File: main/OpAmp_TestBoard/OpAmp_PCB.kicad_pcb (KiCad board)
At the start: 2 copper layers, 145.1 x 56.1 mm, 30 parts, among them U1 LM358

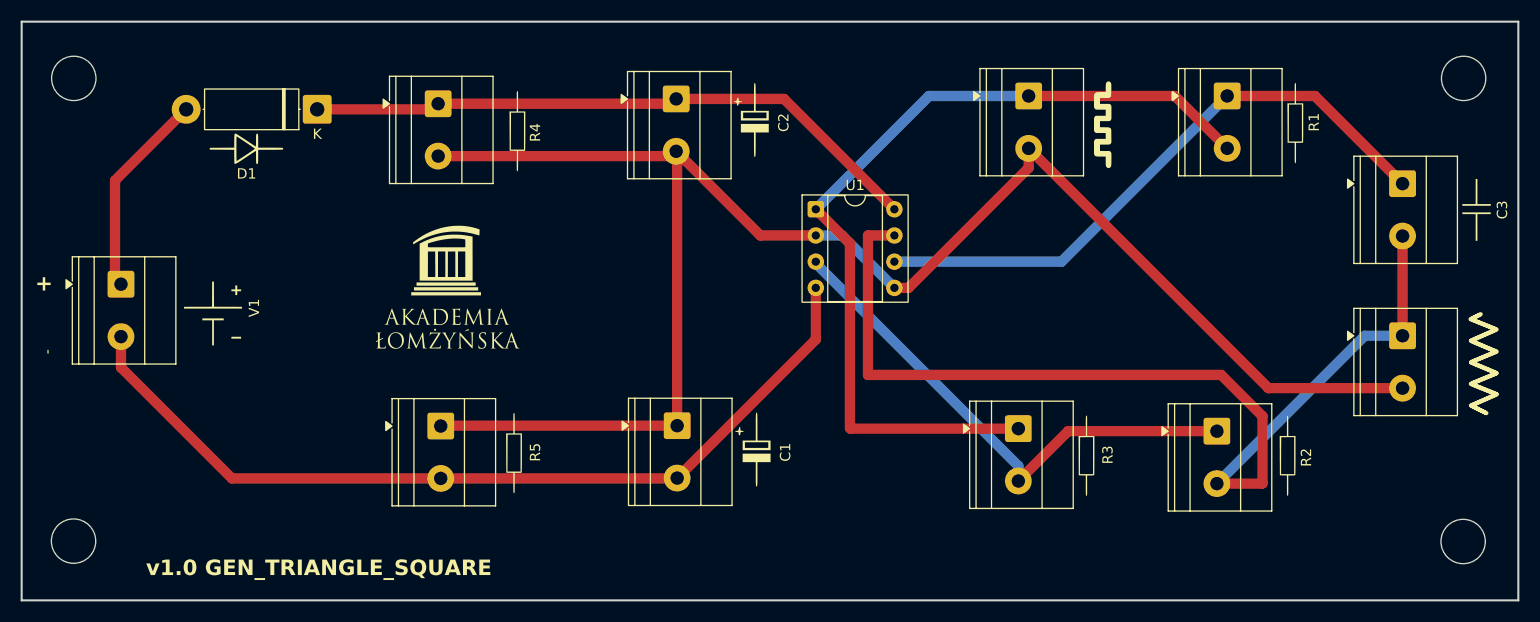
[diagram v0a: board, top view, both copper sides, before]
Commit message: Created new documents folder for Common Emitter Circuit
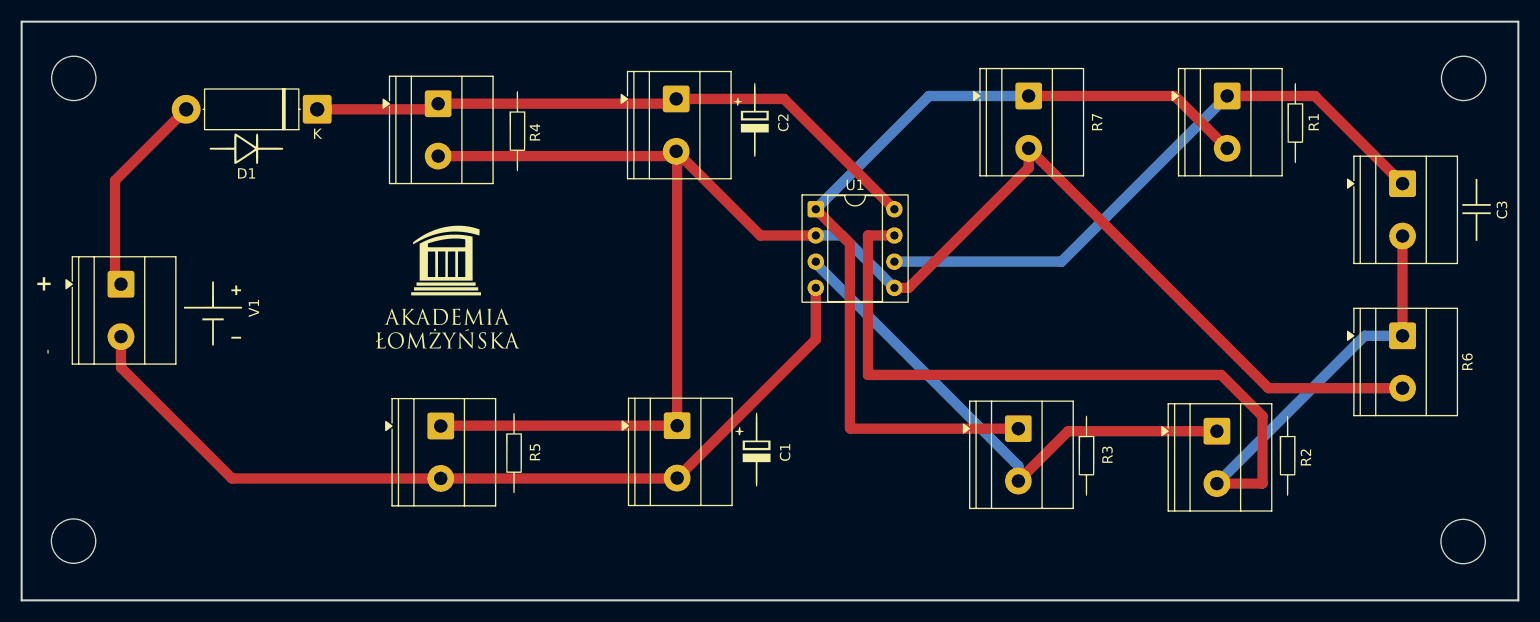
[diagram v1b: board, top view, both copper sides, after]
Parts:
- removed the G*** at (211.0, 74.2)
- removed the G*** at (174.2, 51.0)
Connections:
- net VCC renamed Net-(D1-K)
- C1 pad 1: GNDA -> GND
- C1 pad 2: GND -> Net-(U1-V-)
- C2 pad 2: GNDA -> GND
- R4 pad 2: GNDA -> GND
- R5 pad 1: GNDA -> GND
- R5 pad 2: GND -> Net-(U1-V-)
- R6 pad 2: GNDA -> GND
- R7 pad 2: GNDA -> GND
- U1 pad 2: GNDA -> GND
- U1 pad 4: GND -> Net-(U1-V-)
- U1 pad 5: GNDA -> GND
- V1 pad 2: GND -> Net-(U1-V-)
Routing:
- net GNDA: track 165.1 -> 0.00 mm
- net Net-(U1-V-): track 0.00 -> 85.4 mm
- net GND: track 85.4 -> 165.1 mm
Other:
- board text removed: "v1.0 GEN_TRIANGLE_SQUARE"
